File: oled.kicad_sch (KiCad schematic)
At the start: 4 parts, among them J6 I2C_HEADER

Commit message: Solve all warnings
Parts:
- OLED1: footprint Connector_PinHeader_2.54mm:2.42 OLED Simon Karl Custom -> ksoloti_shield_footprints:128x64OLED_1_3in; symbol ksoloti:display_i2c_oled -> ksoloti_shield_symbols:display_i2c_oled
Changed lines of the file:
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@@
 	)
 	(junction
-		(at 143.51 90.17)
+		(at 143.51 97.79)
 		(diameter 0)
 		(color 0 0 0 0)
@@
 		(color 0 0 0 0)
 	)
-	(junction
-		(at 143.51 97.79)
-		(diameter 0)
-		(color 0 0 0 0)
-	)
-	(junction
-		(at 134.62 90.17)
-		(diameter 0)
-		(color 0 0 0 0)
-	)
 	(no_connect
 		(at 160.02 110.49)
@@
 	(wire
 		(pts
+			(xy 134.62 95.25) (xy 148.59 95.25)
+		)
+		(stroke
+			(width 0)
+			(type default)
+		)
+	)
+	(wire
+		(pts
+			(xy 134.62 90.17) (xy 134.62 95.25)
+		)
+		(stroke
+			(width 0)
+			(type default)
+		)
+	)
+	(wire
+		(pts
+			(xy 114.3 114.3) (xy 113.03 114.3)
+		)
+		(stroke
+			(width 0)
+			(type default)
+		)
+	)
+	(wire
+		(pts
+			(xy 121.92 107.95) (xy 124.46 107.95)
+		)
+		(stroke
+			(width 0)
+			(type default)
+		)
+	)
+	(wire
+		(pts
+			(xy 140.97 102.87) (xy 148.59 102.87)
+		)
+		(stroke
+			(width 0)
+			(type default)
+		)
+	)
+	(wire
+		(pts
 			(xy 130.81 97.79) (xy 143.51 97.79)
 		)
@@
 	(wire
 		(pts
-			(xy 114.3 114.3) (xy 113.03 114.3)
+			(xy 118.11 110.49) (xy 124.46 110.49)
 		)
 		(stroke
@@
 	(wire
 		(pts
-			(xy 121.92 107.95) (xy 124.46 107.95)
-		)
-		(stroke
-			(width 0)
-			(type default)
-		)
-	)
-	(wire
-		(pts
-			(xy 143.51 88.9) (xy 143.51 90.17)
-		)
-		(stroke
-			(width 0)
-			(type default)
-		)
-	)
-	(wire
-		(pts
-			(xy 140.97 102.87) (xy 148.59 102.87)
-		)
-		(stroke
-			(width 0)
-			(type default)
-		)
-	)
-	(wire
-		(pts
-			(xy 134.62 90.17) (xy 134.62 95.25)
-		)
-		(stroke
-			(width 0)
-			(type default)
-		)
-	)
-	(wire
-		(pts
-			(xy 134.62 95.25) (xy 148.59 95.25)
+			(xy 140.97 102.87) (xy 140.97 104.14)
+		)
+		(stroke
+			(width 0)
+			(type default)
+		)
+	)
+	(wire
+		(pts
+			(xy 130.81 95.25) (xy 134.62 95.25)
 		)
 		(stroke
@@
 		(pts
 			(xy 143.51 97.79) (xy 148.59 97.79)
-		)
-		(stroke
-			(width 0)
-			(type default)
-		)
-	)
-	(wire
-		(pts
-			(xy 118.11 110.49) (xy 124.46 110.49)
-		)
-		(stroke
-			(width 0)
-			(type default)
-		)
-	)
-	(wire
-		(pts
-			(xy 134.62 88.9) (xy 134.62 90.17)
-		)
-		(stroke
-			(width 0)
-			(type default)
-		)
-	)
-	(wire
-		(pts
-			(xy 140.97 102.87) (xy 140.97 104.14)
-		)
-		(stroke
-			(width 0)
-			(type default)
-		)
-	)
-	(wire
-		(pts
-			(xy 130.81 95.25) (xy 134.62 95.25)
 		)
 		(stroke
@@
 	)
 	(symbol
-		(lib_id "ksoloti:display_i2c_oled")
+		(lib_id "ksoloti_shield_symbols:display_i2c_oled")
 		(at 148.59 102.87 0)
 		(unit 1)
@@
 			)
 		)
-		(property "Footprint" "Connector_PinHeader_2.54mm:2.42 OLED Simon Karl Custom"
+		(property "Footprint" "ksoloti_shield_footprints:128x64OLED_1_3in"
 			(at 158.75 106.68 0)
 			(effects

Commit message: added OLED footprint and library
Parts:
- OLED1: footprint ksoloti_shield_footprints:128x64OLED_1_3in -> Connector_PinHeader_2.54mm:2.42 OLED Simon Karl Custom
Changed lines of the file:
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@@
 			)
 		)
-		(property "Footprint" "ksoloti_shield_footprints:128x64OLED_1_3in"
+		(property "Footprint" "Connector_PinHeader_2.54mm:2.42 OLED Simon Karl Custom"
 			(at 158.75 106.68 0)
 			(effects

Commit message: Remove symbol copy warnings
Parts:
- OLED1: footprint Connector_PinHeader_2.54mm:2.42 OLED Simon Karl Custom -> ksoloti_shield_footprints:128x64OLED_1_3in
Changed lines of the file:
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@@
 			)
 		)
-		(property "Description" ""
+		(property "Description" "Power symbol creates a global label with name \"GND\" , ground"
 			(at 140.97 104.14 0)
 			(effects
@@
 			)
 		)
-		(property "Description" ""
+		(property "Description" "Power symbol creates a global label with name \"+3.3V\""
 			(at 143.51 82.55 0)
 			(effects
@@
 			)
 		)
-		(property "Description" ""
+		(property "Description" "Power symbol creates a global label with name \"+5V\""
 			(at 146.05 100.33 0)
 			(effects
@@
 			)
 		)
-		(property "Description" ""
+		(property "Description" "Power symbol creates a global label with name \"+3.3V\""
 			(at 134.62 82.55 0)
 			(effects
@@
 			)
 		)
-		(property "Description" ""
+		(property "Description" "Power symbol creates a global label with name \"+5V\""
 			(at 118.11 110.49 0)
 			(effects
@@
 			)
 		)
-		(property "Footprint" "Connector_PinHeader_2.54mm:2.42 OLED Simon Karl Custom"
+		(property "Footprint" "ksoloti_shield_footprints:128x64OLED_1_3in"
 			(at 158.75 106.68 0)
 			(effects
@@
 			)
 		)
-		(property "Description" ""
+		(property "Description" "Power symbol creates a global label with name \"GND\" , ground"
 			(at 113.03 114.3 0)
 			(effects

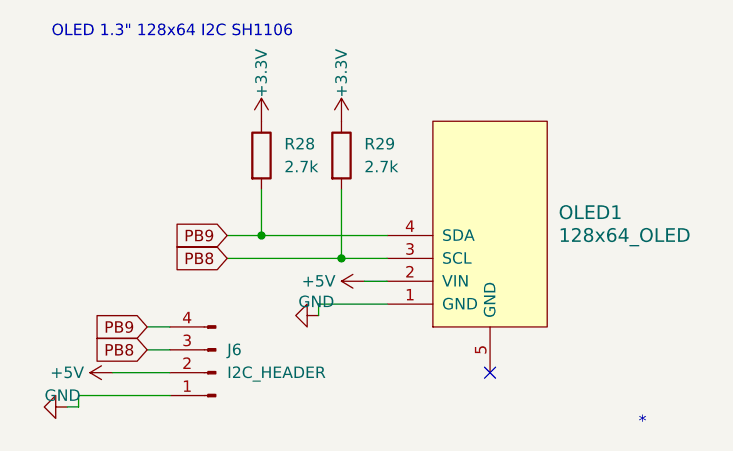
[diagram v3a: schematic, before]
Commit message: Added jack symbols and footprints also footprints for ics and caps
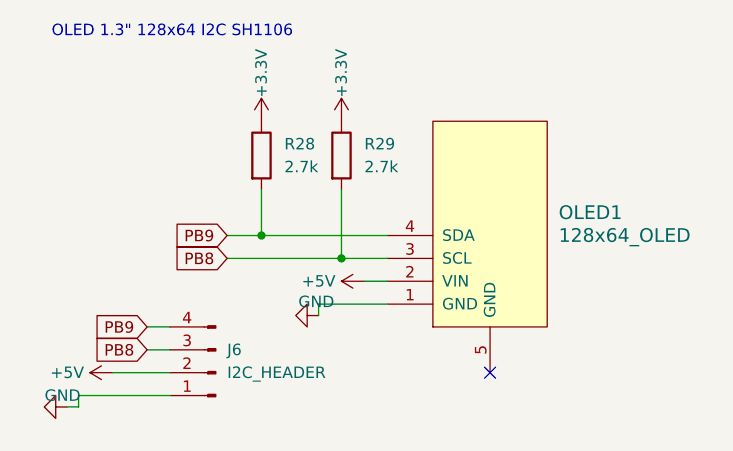
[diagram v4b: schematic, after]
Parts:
- OLED1: footprint ksoloti_shield_footprints:128x64OLED_1_3in -> diggi_footprints:2.42 OLED Simon Karl Custom
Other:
- note removed: "*"
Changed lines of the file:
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@@
-		)
-	)
-	(text "*"
-		(exclude_from_sim no)
-		(at 176.53 116.84 0)
-		(effects
-			(font
-				(size 1.27 1.27)
-			)
-			(justify left bottom)
 		)
 	)
@@
 			)
 		)
-		(property "Footprint" "ksoloti_shield_footprints:128x64OLED_1_3in"
+		(property "Footprint" "diggi_footprints:2.42 OLED Simon Karl Custom"
 			(at 158.75 106.68 0)
 			(effects
